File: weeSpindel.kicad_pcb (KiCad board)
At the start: 2 copper layers, 52.9 x 17.8 mm, 29 parts, among them J1 MPU-6050, J2 USB_B_Micro, SW1 POWER, SW2 RESET, SW3 PROG, U1 ESP-12E, U2 BRCL3130MC, U3 HT7233, U4 CH330N

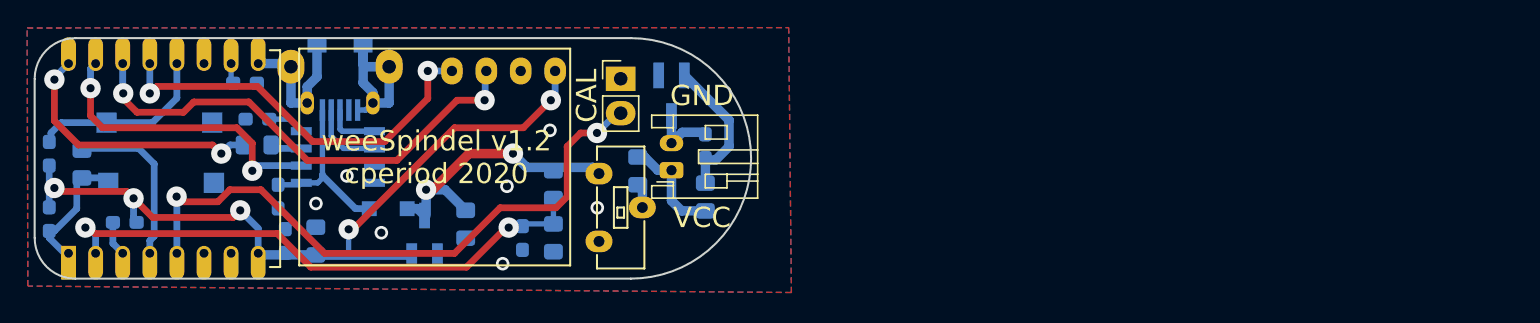
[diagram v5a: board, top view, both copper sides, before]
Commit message: add support for both li-ion and NiMH/Alkaline chemistries, plus USB programming. Among other things.
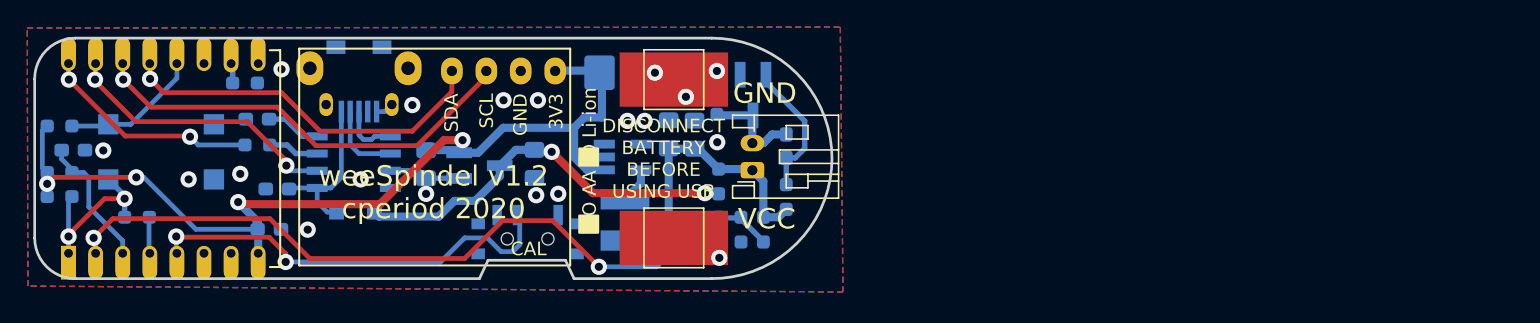
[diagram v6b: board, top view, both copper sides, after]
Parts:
- removed F1: 350mA, Fuse:Fuse_0805_2012Metric_Pad1.15x1.40mm_HandSolder
- removed SW1: POWER, CPB:SPST Switch 9mmx3.5mm C223839
- added C10: 22u, Capacitor_SMD:C_0805_2012Metric_Pad1.18x1.45mm_HandSolder, B.Cu at (139.7, 103.1)
- added C11: 150u, Capacitor_Tantalum_SMD:CP_EIA-7343-20_Kemet-V_Pad2.25x2.55mm_HandSolder, B.Cu at (135.9, 98.6)
- added C7: 22u, Capacitor_SMD:C_0805_2012Metric_Pad1.18x1.45mm_HandSolder, B.Cu at (127.9, 105.3)
- added C9: 100n, Capacitor_SMD:C_0603_1608Metric_Pad1.08x0.95mm_HandSolder, B.Cu at (93.9, 104.3)
- added L1: 10uH, Inductor_SMD:L_Bourns-SRN4018, B.Cu at (134.6, 109.4)
- added R10: 0R, Resistor_SMD:R_0603_1608Metric_Pad0.98x0.95mm_HandSolder, B.Cu at (141.4, 100.7)
- added R11: 0R, Resistor_SMD:R_0603_1608Metric_Pad0.98x0.95mm_HandSolder, B.Cu at (141.5, 106.6)
- added TP1: TestPoint, TestPoint:TestPoint_Pad_4.0x4.0mm, F.Cu at (138.2, 99.1)
- added TP2: TestPoint, TestPoint:TestPoint_Pad_4.0x4.0mm, F.Cu at (138.2, 110.7)
- added U5: HT7733SA, Package_TO_SOT_SMD:SOT-23-5_HandSoldering, B.Cu at (134.4, 104.8)
- BT1: value Li 3.7v -> 1.2V-4.2V
- C1, C4, C5, C6, C8: value 100nF -> 100n; footprint Capacitor_SMD:C_0603_1608Metric_Pad1.05x0.95mm_HandSolder -> Capacitor_SMD:C_0603_1608Metric_Pad1.08x0.95mm_HandSolder
- C2: value 10uF -> 22u; footprint Capacitor_SMD:C_0805_2012Metric_Pad1.15x1.40mm_HandSolder -> Capacitor_SMD:C_0805_2012Metric_Pad1.18x1.45mm_HandSolder
- C3: value 22uF -> 22u; footprint Capacitor_SMD:C_0805_2012Metric_Pad1.15x1.40mm_HandSolder -> Capacitor_SMD:C_0805_2012Metric_Pad1.18x1.45mm_HandSolder
- JP1: footprint CPB:Socket_Strip_Straight_1x02_Oval_Pitch2.54mm -> Button_Switch_SMD:SW_SPDT_PCM12; moved to B.Cu
- R1, R2, R3, R8, R9: footprint Resistor_SMD:R_0805_2012Metric_Pad1.15x1.40mm_HandSolder -> Resistor_SMD:R_0603_1608Metric_Pad0.98x0.95mm_HandSolder
- R4, R5, R6, R7: footprint Resistor_SMD:R_0603_1608Metric_Pad1.05x0.95mm_HandSolder -> Resistor_SMD:R_0603_1608Metric_Pad0.98x0.95mm_HandSolder
- moved C2 16.4 mm to (137.8, 103.1), turned to 90 degrees
- moved R1 15.8 mm to (144.8, 110.1)
- moved C6 14.5 mm to (141.5, 110.1)
- moved R2 13.9 mm to (143.1, 110.1)
- moved JP1 13.4 mm to (127.4, 110.5), turned to 180 degrees
- moved C3 9.92 mm to (119.9, 105.3), turned to -90 degrees
- moved U3 6.58 mm to (123.8, 105.4), turned to 0 degrees
- moved R6 6.06 mm to (92.8, 105.9), turned to 180 degrees
- moved U2 6.02 mm to (144.0, 100.2)
- moved BT1 5.97 mm to (144.0, 105.8)
- moved C4 5.97 mm to (146.5, 104.0)
- moved R8 5.97 mm to (146.5, 107.7)
- moved R3 5.65 mm to (98.6, 109.2), turned to 180 degrees
- moved D1 2.43 mm to (114.7, 108.8)
- moved R4 2.18 mm to (92.8, 102.5), turned to 180 degrees
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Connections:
- net 3V3 renamed +3V3
- net Net-(J2-Pad2) renamed /D-
- net Net-(J2-Pad3) renamed /D+
- net Net-(JP1-Pad2) renamed /CAL
- net Net-(R3-Pad1) renamed /IO16
- net Net-(R3-Pad2) renamed /RST
- net Net-(R4-Pad1) renamed /IO0
- net Net-(R6-Pad1) renamed /EN
- net Net-(R7-Pad2) renamed /IO15
- BT1 pad 1: Net-(BT1-Pad1) -> +BATT
- C2 pad 1: +5V -> +BATT
- D1 pad 1: +5V -> VBUS
- J2 pad 4: Net-(J2-Pad4) -> unconnected-(J2-Pad4)
- R1 pad 2: +5V -> +BATT
- R8 pad 2: Net-(BT1-Pad1) -> +BATT
- U1 pad 11: Net-(U1-Pad11) -> unconnected-(U1-Pad11)
- U1 pad 6: Net-(U1-Pad6) -> unconnected-(U1-Pad6)
- U1 pad 7: Net-(U1-Pad7) -> unconnected-(U1-Pad7)
- U3 pad 3: +5V -> VBUS
- U4 pad 4: Net-(U4-Pad4) -> unconnected-(U4-Pad4)
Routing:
- net VBUS: track 0.00 -> 29.4 mm, vias 0 -> 2
- net +BATT: track 0.00 -> 22.0 mm
- net +5V: track 21.4 -> 0.00 mm, vias 2 -> 0
- net GND: track 23.2 -> 6.65 mm, vias 7 -> 19
- net ADC: track 41.3 -> 57.4 mm
- net /CAL: track 45.9 -> 31.4 mm
- net +3V3: track 61.1 -> 73.5 mm, vias 5 -> 4
- net /IO16: track 12.5 -> 2.69 mm
- net Net-(BT1-Pad1): track 7.96 -> 0.00 mm
- net /EN: track 2.63 -> 9.99 mm
- net eTX: track 19.9 -> 16.2 mm
- net /RST: track 9.65 -> 13.2 mm, vias 0 -> 2
- net SCL: track 35.9 -> 32.5 mm, vias 2 -> 1
- net /IO0: track 13.5 -> 10.3 mm
- net Net-(BT1-Pad2): track 4.68 -> 7.46 mm
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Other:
- board size 52.9 x 17.8 mm -> 58.8 x 17.8 mm
- net class Default removed
- board text added: "3V3"
- board text added: "DISCONNECT BATTERY BEFORE USING USB"
- board text added: "O AA O Li-ion"
- board text added: "SCL"
- board text added: "SDA"
- board text removed: "BATTERY OFF BEFORE USB"

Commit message: some more tidying. ground plane is actually more of a plane now.
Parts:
- R3: value 1K -> 470R
- moved R3 5.75 mm to (92.8, 109.5)
- moved D1 2.17 mm to (114.5, 111.0)
- moved C1 1.89 mm to (107.4, 108.5), turned to 0 degrees
- moved C10 1.71 mm to (139.7, 104.8)
- moved C2 1.71 mm to (137.8, 104.8)
- moved C8 1.58 mm to (107.4, 106.7)
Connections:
- SW2 pad 1: /RST -> /EN
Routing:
- net /RST: track 13.2 -> 5.70 mm, vias 2 -> 0
- net /IO16: track 2.69 -> 7.55 mm, vias 0 -> 2
- net +3V3: track 73.5 -> 77.1 mm
- net Net-(C8-Pad1): track 11.8 -> 15.3 mm
- net +BATT: track 22.0 -> 19.8 mm
- net /EN: track 9.99 -> 11.0 mm
- net ADC: track 57.4 -> 58.3 mm
- net VBUS: track 29.4 -> 30.2 mm
- net SDA: track 27.7 -> 27.1 mm
- net GND: vias 19 -> 26
